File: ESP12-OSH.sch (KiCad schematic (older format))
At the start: 14 parts, among them P1 CONN_01X08, P2 CONN_01X06, P3 CONN_01X08, P4 CONN_01X02, U2 ESP-12E, U3 SPX2920U-3.3

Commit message: headers with 2.54mm spacing
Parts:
- JP1, JP2, P4: footprint Pin_Headers:Pin_Header_Straight_1x02_Pitch2.00mm -> Pin_Headers:Pin_Header_Straight_1x02_Pitch2.54mm
- P1, P3: footprint Pin_Headers:Pin_Header_Straight_1x08_Pitch2.00mm -> Pin_Headers:Pin_Header_Straight_1x08_Pitch2.54mm
- P2: footprint Pin_Headers:Pin_Header_Straight_1x06_Pitch2.00mm -> Pin_Headers:Pin_Header_Straight_1x06_Pitch2.54mm
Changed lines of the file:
@@
 F 0 "P1" H 2975 3625 50  0000 C CNN
 F 1 "CONN_01X08" H 2775 3550 50  0000 C CNN
-F 2 "Pin_Headers:Pin_Header_Straight_1x08_Pitch2.00mm" H 2950 3100 50  0001 C CNN
+F 2 "Pin_Headers:Pin_Header_Straight_1x08_Pitch2.54mm" H 2950 3100 50  0001 C CNN
 F 3 "" H 2950 3100 50  0000 C CNN
 	1    2950 3100
@@
 F 0 "P2" V 4800 3950 50  0000 L CNN
 F 1 "CONN_01X06" V 4875 3950 50  0000 L CNN
-F 2 "Pin_Headers:Pin_Header_Straight_1x06_Pitch2.00mm" H 4700 4250 50  0001 C CNN
+F 2 "Pin_Headers:Pin_Header_Straight_1x06_Pitch2.54mm" H 4700 4250 50  0001 C CNN
 F 3 "" H 4700 4250 50  0000 C CNN
 	1    4700 4250
@@
 F 0 "JP1" H 3500 2864 50  0000 C CNN
 F 1 "Jumper" H 3500 2773 50  0000 C CNN
-F 2 "Pin_Headers:Pin_Header_Straight_1x02_Pitch2.00mm" H 3500 2600 50  0001 C CNN
+F 2 "Pin_Headers:Pin_Header_Straight_1x02_Pitch2.54mm" H 3500 2600 50  0001 C CNN
 F 3 "" H 3500 2600 50  0000 C CNN
 	1    3500 2600
@@
 F 0 "JP2" H 5775 5164 50  0000 C CNN
 F 1 "Jumper" H 5775 5073 50  0000 C CNN
-F 2 "Pin_Headers:Pin_Header_Straight_1x02_Pitch2.00mm" H 5775 4900 50  0001 C CNN
+F 2 "Pin_Headers:Pin_Header_Straight_1x02_Pitch2.54mm" H 5775 4900 50  0001 C CNN
 F 3 "" H 5775 4900 50  0000 C CNN
 	1    5775 4900
@@
 F 0 "P3" H 6300 2575 50  0000 L CNN
 F 1 "CONN_01X08" H 5900 2650 50  0000 L CNN
-F 2 "Pin_Headers:Pin_Header_Straight_1x08_Pitch2.00mm" H 6325 3100 50  0001 C CNN
+F 2 "Pin_Headers:Pin_Header_Straight_1x08_Pitch2.54mm" H 6325 3100 50  0001 C CNN
 F 3 "" H 6325 3100 50  0000 C CNN
 	1    6325 3100
@@
 F 0 "P4" V 3525 4800 50  0000 C CNN
 F 1 "CONN_01X02" V 3425 4800 50  0000 C CNN
-F 2 "Pin_Headers:Pin_Header_Straight_1x02_Pitch2.00mm" H 3325 4800 50  0001 C CNN
+F 2 "Pin_Headers:Pin_Header_Straight_1x02_Pitch2.54mm" H 3325 4800 50  0001 C CNN
 F 3 "" H 3325 4800 50  0000 C CNN
 	1    3325 4800

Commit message: extra small cap, moved large cap, removed front zone VCC, removed vias, moved parts around, added mounting holes
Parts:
- removed U3: SPX2920U-3.3, Power_Integrations:TO-220, symbol SPX2920U-3.3
- added C1: 100nF, Capacitors_THT:C_Disc_D3.0mm_W1.6mm_P2.50mm, symbol C
- added H1: HT7333, TO_SOT_Packages_THT:TO-92_Inline_Narrow_Oval, symbol HT7333
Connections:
- wire segments 39 -> 42
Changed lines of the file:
@@
 LIBS:contrib
 LIBS:valves
+LIBS:ESP12-OSH
+LIBS:ht7333
 LIBS:ESP12-OSH-cache
 EELAYER 25 0
@@
 Wire Wire Line
 	2975 4600 3275 4600
-$Comp
-L SPX2920U-3.3 U3
-U 1 1 58B6B952
-P 3375 4200
-F 0 "U3" H 3150 4575 50  0000 C CNN
-F 1 "SPX2920U-3.3" H 3375 4500 50  0000 C CNN
-F 2 "Power_Integrations:TO-220" H 3375 4426 50  0000 C CIN
-F 3 "" H 3375 4200 50  0000 C CNN
-	1    3375 4200
-	1    0    0    -1
-$EndComp
-Wire Wire Line
-	3375 4450 3375 4600
+Wire Wire Line
+	3375 4350 3375 4600
 Wire Wire Line
 	2975 4150 2975 4600
@@
 $EndComp
 Wire Wire Line
-	3825 4150 3775 4150
+	3625 4150 3825 4150
 Wire Wire Line
 	3825 4150 3825 4250
@@
 Connection ~ 3200 2750
 Connection ~ 3200 2600
+$Comp
+L C C1
+U 1 1 58BC6047
+P 3700 3625
+F 0 "C1" H 3475 3625 50  0000 L CNN
+F 1 "100nF" H 3475 3550 50  0000 L CNN
+F 2 "Capacitors_THT:C_Disc_D3.0mm_W1.6mm_P2.50mm" H 3738 3475 50  0001 C CNN
+F 3 "" H 3700 3625 50  0000 C CNN
+	1    3700 3625
+	1    0    0    -1
+$EndComp
+Wire Wire Line
+	3700 3775 3975 3775
+Text Label 3800 3775 0    60   ~ 0
+GND
+$Comp
+L HT7333 H1
+U 1 1 58BC6BB5
+P 3475 3800
+F 0 "H1" H 3685 3920 60  0000 C CNN
+F 1 "HT7333" H 3575 4000 60  0000 C CNN
+F 2 "TO_SOT_Packages_THT:TO-92_Inline_Narrow_Oval" H 3475 3800 60  0001 C CNN
+F 3 "" H 3475 3800 60  0001 C CNN
+	1    3475 3800
+	-1   0    0    1
+$EndComp
+Wire Wire Line
+	3125 4150 2975 4150
+Wire Wire Line
+	3700 3475 3700 3450
+Connection ~ 3700 3450
 $EndSCHEMATC

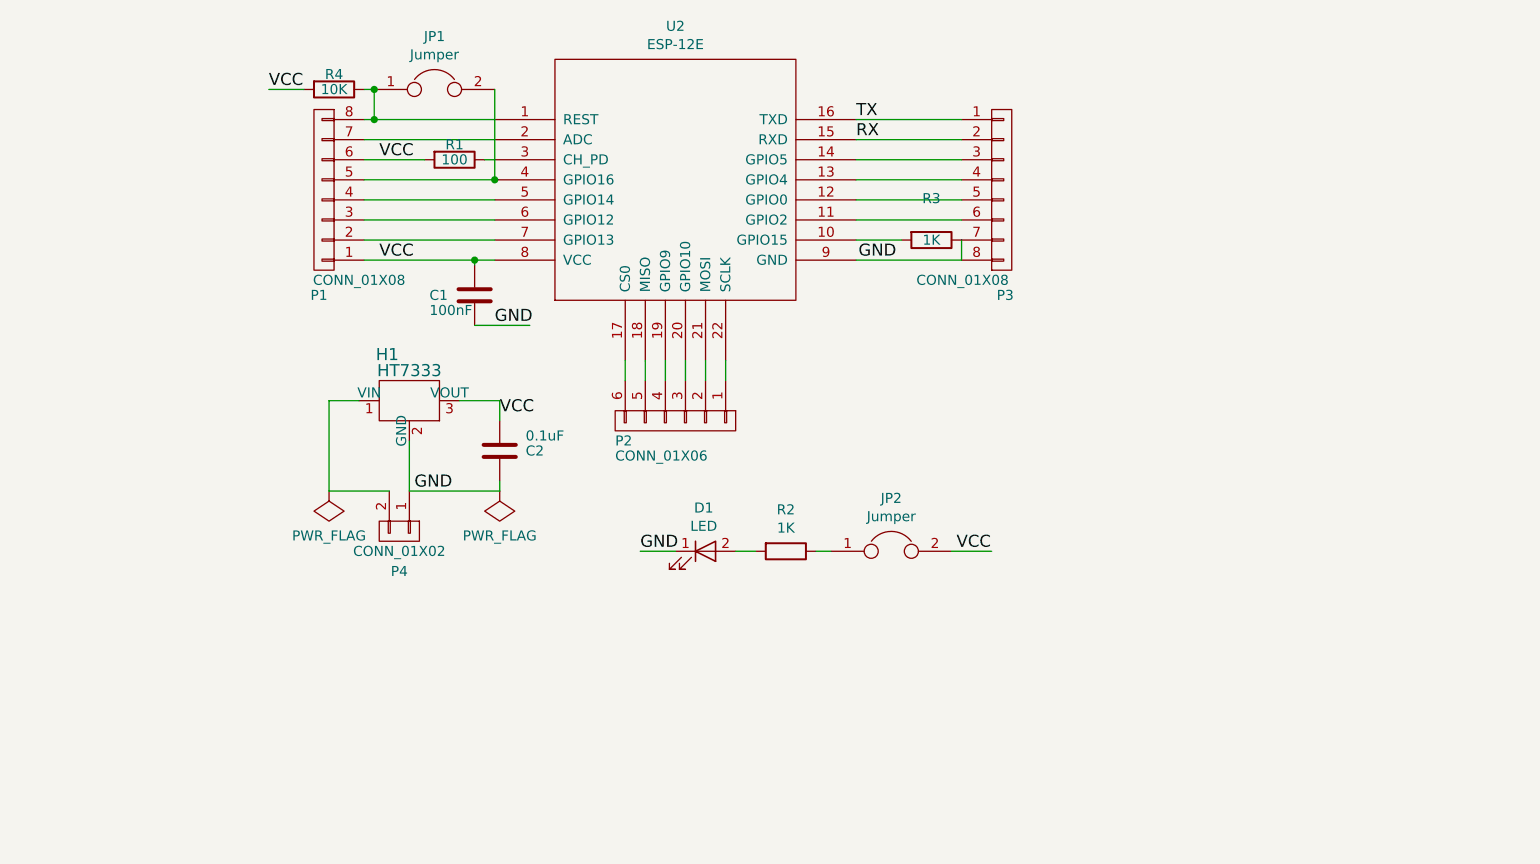
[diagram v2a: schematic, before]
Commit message: switches for control and start with voltage divider for battery capacity management
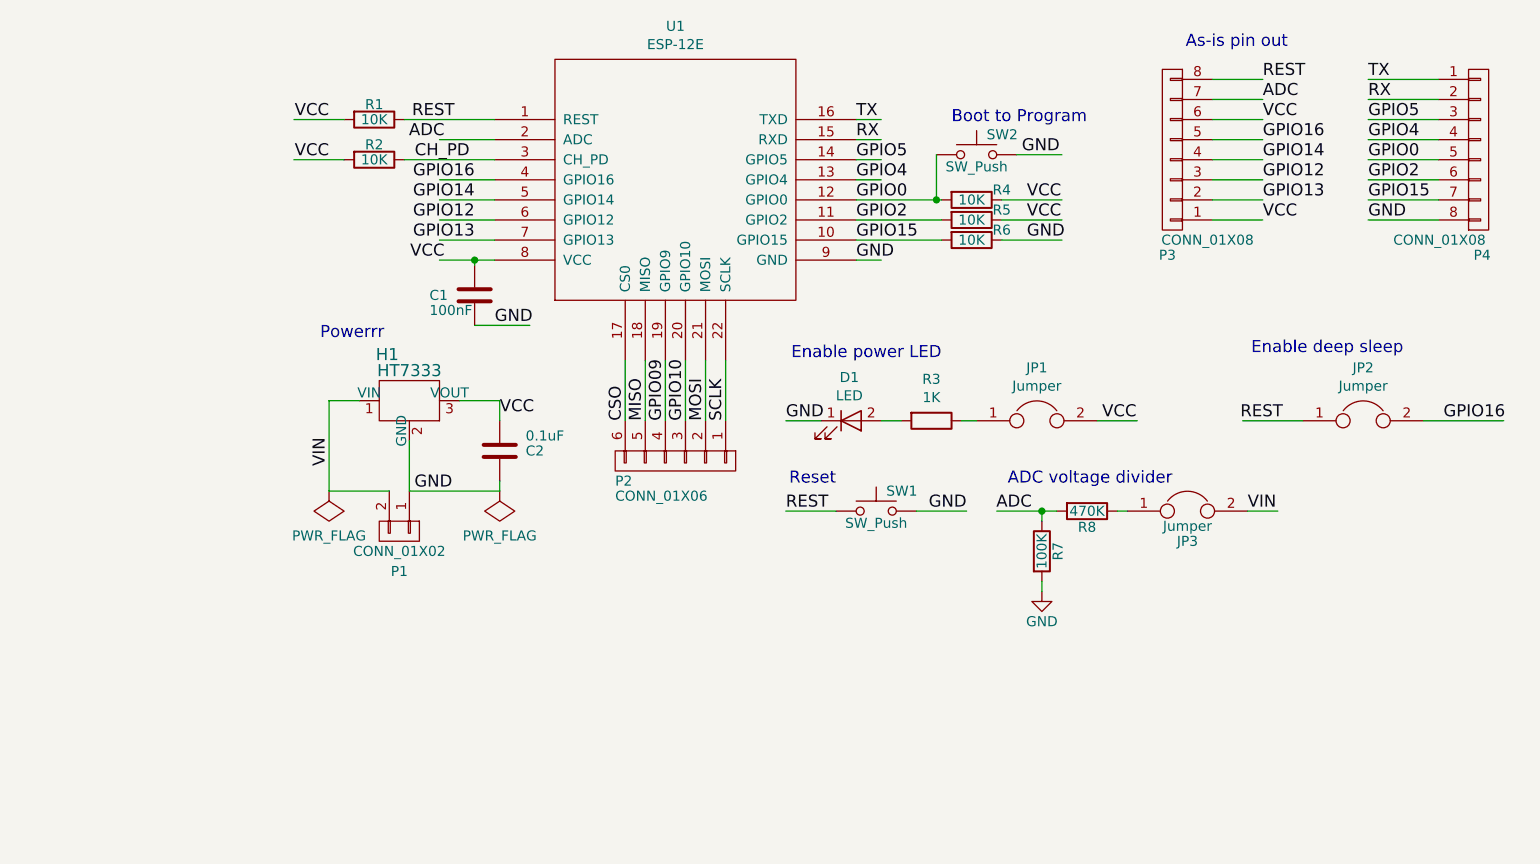
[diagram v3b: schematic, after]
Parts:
- removed JP1: Jumper, Pin_Headers:Pin_Header_Straight_1x02_Pitch2.54mm, symbol Jumper
- added JP2, JP3: Jumper, Pin_Headers:Pin_Header_Straight_1x02_Pitch2.54mm, symbol Jumper
- added R4, R5: 10K, Resistors_THT:R_Axial_DIN0207_L6.3mm_D2.5mm_P7.62mm_Horizontal, symbol R
- added R7: 100K, Resistors_THT:R_Axial_DIN0207_L6.3mm_D2.5mm_P7.62mm_Horizontal, symbol R
- added R8: 470K, Resistors_THT:R_Axial_DIN0207_L6.3mm_D2.5mm_P7.62mm_Horizontal, symbol R
- added SW1, SW2: SW_Push, Buttons_Switches_THT:SW_PUSH_6mm, symbol SW_Push
- R2: renamed from R1; value 100 -> 10K
- R6: renamed from R3; value 1K -> 10K
- renumbered JP2 to JP1, P4 to P1, P1 to P3, P3 to P4, R4 to R1, R2 to R3, U2 to U1
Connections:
- net labels added: ADC, CH_PD, CSO, GPIO0, GPIO09, GPIO10, GPIO12, GPIO13, GPIO14, GPIO15, GPIO16, GPIO2, GPIO4, GPIO5, MISO, MOSI, REST, SCLK, VIN
- wire segments 42 -> 68
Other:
- note added: "ADC voltage divider"
- note added: "As-is pin out"
- note added: "Boot to Program"
- note added: "Enable deep sleep"
- note added: "Enable power LED"
- note added: "Powerrr"
- note added: "Reset"
- moved on the sheet: D1, JP1, P2, P3, P4, R1, R2, R3, R6

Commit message: version 2 in the works!
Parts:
- H1: footprint TO_SOT_Packages_THT:TO-92_Inline_Narrow_Oval -> TO_SOT_Packages_THT:TO-92_Inline_Wide
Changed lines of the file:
@@
 EESchema Schematic File Version 2
 LIBS:ESP12-OSH-rescue
+LIBS:power
+LIBS:device
+LIBS:transistors
+LIBS:conn
+LIBS:linear
+LIBS:regul
+LIBS:74xx
+LIBS:cmos4000
+LIBS:adc-dac
+LIBS:memory
+LIBS:xilinx
+LIBS:microcontrollers
+LIBS:dsp
+LIBS:microchip
+LIBS:analog_switches
+LIBS:motorola
+LIBS:texas
+LIBS:intel
+LIBS:audio
+LIBS:interface
+LIBS:digital-audio
+LIBS:philips
+LIBS:display
+LIBS:cypress
+LIBS:siliconi
+LIBS:opto
+LIBS:atmel
+LIBS:contrib
+LIBS:valves
 LIBS:ESP12-OSH
 LIBS:ht7333
+LIBS:switches
+LIBS:ftdi
 LIBS:ESP12-OSH-cache
 EELAYER 25 0
@@
 F 0 "H1" H 3685 3920 60  0000 C CNN
 F 1 "HT7333" H 3575 4000 60  0000 C CNN
-F 2 "TO_SOT_Packages_THT:TO-92_Inline_Narrow_Oval" H 3475 3800 60  0001 C CNN
+F 2 "TO_SOT_Packages_THT:TO-92_Inline_Wide" H 3475 3800 60  0001 C CNN
 F 3 "" H 3475 3800 60  0001 C CNN
 	1    3475 3800

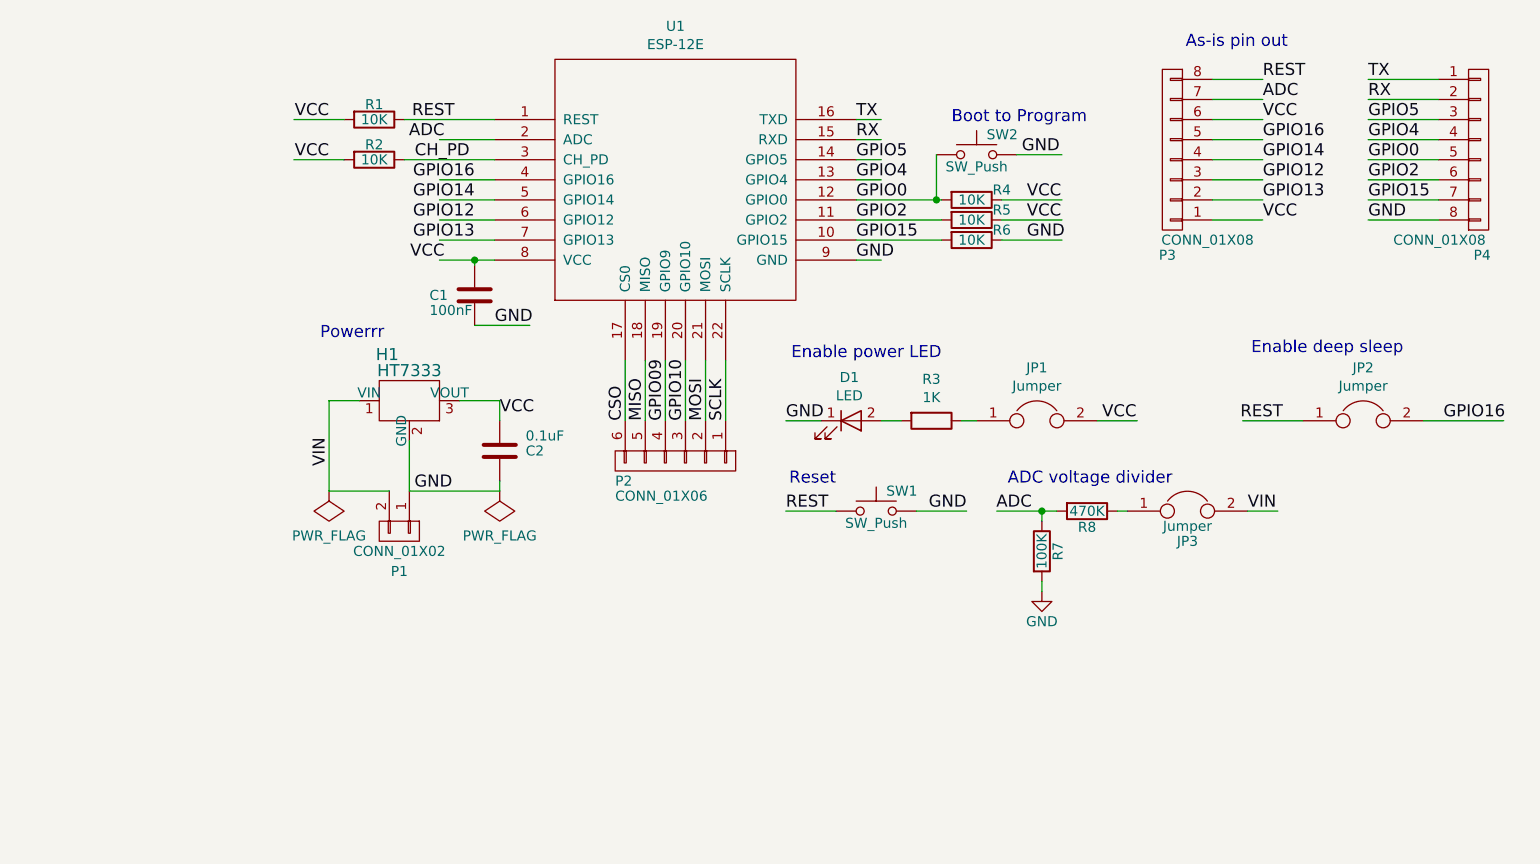
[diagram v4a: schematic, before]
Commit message: thicker traces, antenna outside of pcb, shorter traces, removed custom HT7333 footprint
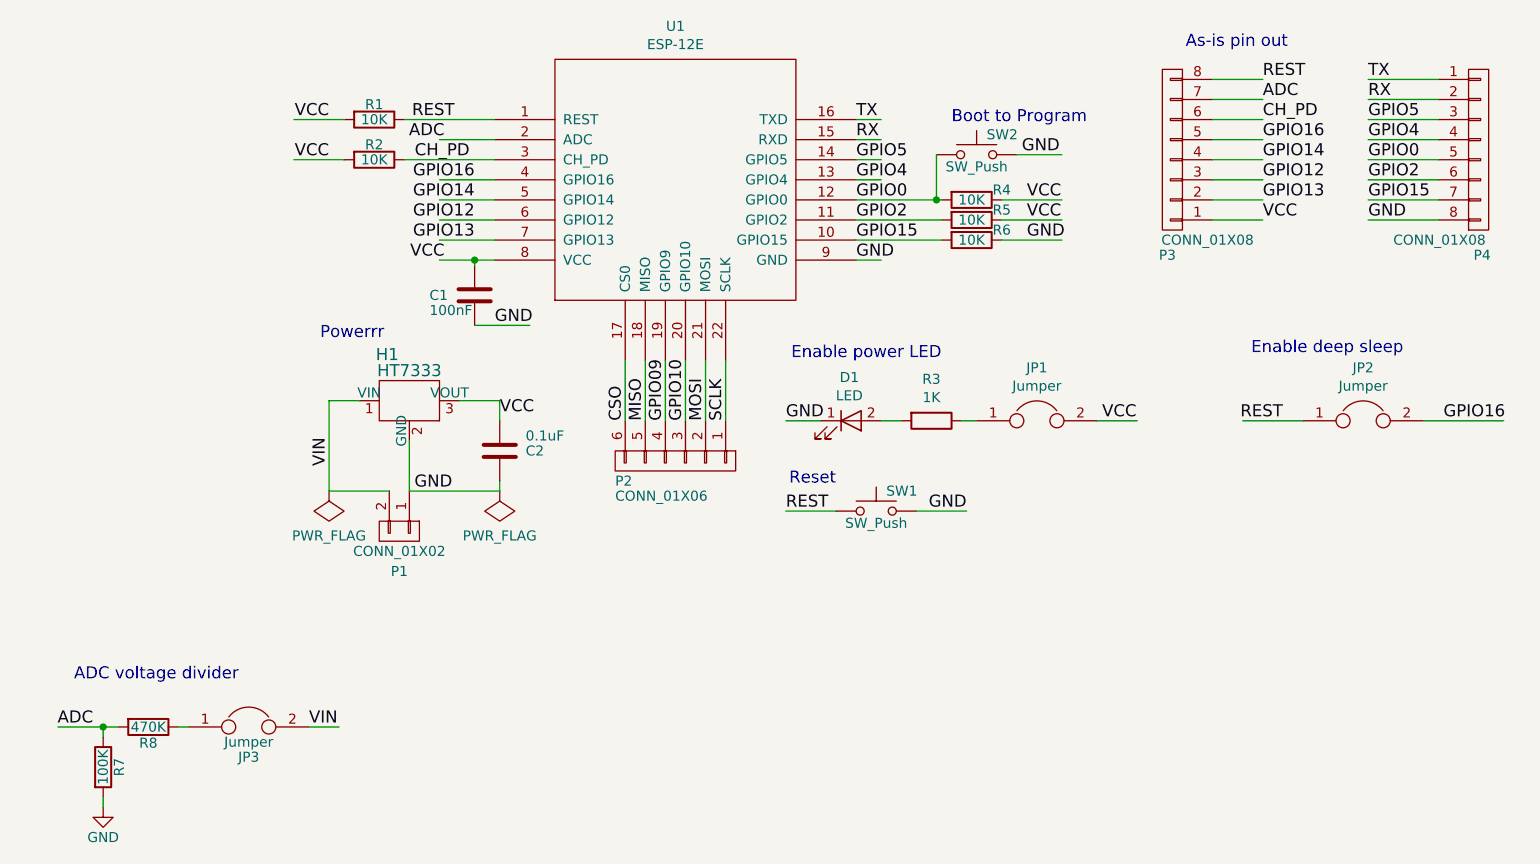
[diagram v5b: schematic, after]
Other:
- moved on the sheet: JP3, R7, R8
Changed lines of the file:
@@
 LIBS:valves
 LIBS:ESP12-OSH
-LIBS:ht7333
 LIBS:switches
 LIBS:ftdi
@@
 Text Label 7625 2650 0    60   ~ 0
 ADC
-Text Label 7625 2750 0    60   ~ 0
-VCC
 Text Label 7625 2850 0    60   ~ 0
 GPIO16
@@
 Text Notes 8325 3925 2    60   ~ 0
 Enable deep sleep
-Text Notes 7175 4575 2    60   ~ 0
+Text Notes 2525 5550 2    60   ~ 0
 ADC voltage divider
-Text Label 6475 4700 2    60   ~ 0
+Text Label 1800 5775 2    60   ~ 0
 ADC
 Text Label 2975 4475 1    60   ~ 0
 VIN
-Text Label 7550 4700 0    60   ~ 0
+Text Label 2875 5775 0    60   ~ 0
 VIN
 $Comp
 L Jumper JP3
 U 1 1 58D45376
-P 7250 4700
-F 0 "JP3" H 7250 4550 50  0000 C CNN
-F 1 "Jumper" H 7250 4625 50  0000 C CNN
-F 2 "Pin_Headers:Pin_Header_Straight_1x02_Pitch2.54mm" H 7250 4700 50  0001 C CNN
-F 3 "" H 7250 4700 50  0000 C CNN
-	1    7250 4700
+P 2575 5775
+F 0 "JP3" H 2575 5625 50  0000 C CNN
+F 1 "Jumper" H 2575 5700 50  0000 C CNN
+F 2 "Pin_Headers:Pin_Header_Straight_1x02_Pitch2.54mm" H 2575 5775 50  0001 C CNN
+F 3 "" H 2575 5775 50  0000 C CNN
+	1    2575 5775
 	1    0    0    -1
 $EndComp
@@
 L R R8
 U 1 1 58D454B0
-P 6750 4700
-F 0 "R8" V 6830 4700 50  0000 C CNN
-F 1 "470K" V 6750 4700 50  0000 C CNN
-F 2 "Resistors_THT:R_Axial_DIN0207_L6.3mm_D2.5mm_P7.62mm_Horizontal" V 6680 4700 50  0001 C CNN
-F 3 "" H 6750 4700 50  0001 C CNN
-	1    6750 4700
+P 2075 5775
+F 0 "R8" V 2155 5775 50  0000 C CNN
+F 1 "470K" V 2075 5775 50  0000 C CNN
+F 2 "Resistors_THT:R_Axial_DIN0207_L6.3mm_D2.5mm_P7.62mm_Horizontal" V 2005 5775 50  0001 C CNN
+F 3 "" H 2075 5775 50  0001 C CNN
+	1    2075 5775
 	0    1    1    0
 $EndComp
@@
 L R R7
 U 1 1 58D45514
-P 6525 4900
-F 0 "R7" V 6605 4900 50  0000 C CNN
-F 1 "100K" V 6525 4900 50  0000 C CNN
-F 2 "Resistors_THT:R_Axial_DIN0207_L6.3mm_D2.5mm_P7.62mm_Horizontal" V 6455 4900 50  0001 C CNN
-F 3 "" H 6525 4900 50  0001 C CNN
-	1    6525 4900
+P 1850 5975
+F 0 "R7" V 1930 5975 50  0000 C CNN
+F 1 "100K" V 1850 5975 50  0000 C CNN
+F 2 "Resistors_THT:R_Axial_DIN0207_L6.3mm_D2.5mm_P7.62mm_Horizontal" V 1780 5975 50  0001 C CNN
+F 3 "" H 1850 5975 50  0001 C CNN
+	1    1850 5975
 	1    0    0    -1
 $EndComp
@@
 L GND-RESCUE-ESP12-OSH #PWR03
 U 1 1 58D457AB
-P 6525 5100
-F 0 "#PWR03" H 6525 4850 50  0001 C CNN
-F 1 "GND" H 6525 4950 50  0000 C CNN
-F 2 "" H 6525 5100 50  0001 C CNN
-F 3 "" H 6525 5100 50  0001 C CNN
-	1    6525 5100
-	1    0    0    -1
-$EndComp
-Wire Wire Line
-	6525 5050 6525 5100
-Wire Wire Line
-	7550 4700 7700 4700
-Wire Wire Line
-	6950 4700 6900 4700
-Wire Wire Line
-	6300 4700 6600 4700
-Wire Wire Line
-	6525 4750 6525 4700
-Connection ~ 6525 4700
+P 1850 6175
+F 0 "#PWR03" H 1850 5925 50  0001 C CNN
+F 1 "GND" H 1850 6025 50  0000 C CNN
+F 2 "" H 1850 6175 50  0001 C CNN
+F 3 "" H 1850 6175 50  0001 C CNN
+	1    1850 6175
+	1    0    0    -1
+$EndComp
+Wire Wire Line
+	1850 6125 1850 6175
+Wire Wire Line
+	2875 5775 3025 5775
+Wire Wire Line
+	1625 5775 1925 5775
+Wire Wire Line
+	1850 5825 1850 5775
+Connection ~ 1850 5775
 Text Notes 3250 3850 2    60   ~ 0
 Powerrr
 Text Notes 7750 2400 2    60   ~ 0
 As-is pin out
+Wire Wire Line
+	2275 5775 2225 5775
+Text Label 7625 2750 0    60   ~ 0
+CH_PD
 $EndSCHEMATC
